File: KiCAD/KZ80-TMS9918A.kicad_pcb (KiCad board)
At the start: 2 copper layers, 100 x 75 mm, 43 parts, among them J1 Conn_Coaxial, J2 SBC8080 BUS, J3 EXT_JP, J4 AD_JP, J5 AD_JP, Q1 2SC1815, U1 74HCT04, U2 74HC139, U3 74HC32, U4 TMS9918A, U5 74HCT04, U6 74HCT574, U7 74HCT574, U8 HM62256, U9 74HCT574, Y1 10.738635MHZ

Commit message: 64k DRAM版 ガーバー出力
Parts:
- removed C15: 470u, Capacitor_THT:CP_Radial_D8.0mm_P3.50mm
- removed the C3 at (139.0, 97.5)
- removed the C4 at (113.5, 94.5)
- removed the C5 at (141.0, 67.5)
- removed the JP1 at (162.0, 105.5)
- removed the U3 at (188.5, 100.5)
- removed U9: 74HCT574, Package_DIP:DIP-20_W7.62mm_Socket
- added C1: 10u, Capacitor_THT:CP_Radial_D5.0mm_P2.50mm, F.Cu at (104.8, 93.5)
- added C14: 0.1u, Capacitor_THT:C_Disc_D3.0mm_W1.6mm_P2.50mm, F.Cu at (197.5, 103.6)
- added C2: 0.1u, Capacitor_THT:C_Disc_D3.0mm_W1.6mm_P2.50mm, F.Cu at (119.0, 66.9)
- added JP2: A7_JP, Connector_PinHeader_2.54mm:PinHeader_1x03_P2.54mm_Vertical, F.Cu at (178.3, 76.9)
- added U4: 74HCT04, Package_DIP:DIP-14_W7.62mm_Socket, F.Cu at (121.8, 86.6)
- C12: value 0.1u -> 10u; footprint Capacitor_THT:C_Disc_D3.0mm_W1.6mm_P2.50mm -> Capacitor_THT:CP_Radial_D5.0mm_P2.50mm
- C13: value 10u -> 0.1u; footprint Capacitor_THT:CP_Radial_D5.0mm_P2.50mm -> Capacitor_THT:C_Disc_D3.0mm_W1.6mm_P2.50mm
- C7: value 0.1u -> 470u; footprint Capacitor_THT:C_Disc_D3.0mm_W1.6mm_P2.50mm -> Capacitor_THT:CP_Radial_D5.0mm_P2.50mm
- L1: value L_Core_Ferrite -> L_Ferrite_Small; footprint Inductor_THT:L_Axial_L5.3mm_D2.2mm_P10.16mm_Horizontal_Vishay_IM-1 -> Resistor_THT:R_Axial_DIN0207_L6.3mm_D2.5mm_P10.16mm_Horizontal
- U1: value 74HCT04 -> 74HCT32
- U2: value 74HC139 -> 74HCT04; footprint Package_DIP:DIP-16_W7.62mm_Socket -> Package_DIP:DIP-14_W7.62mm_Socket
- U5: value 74HCT04 -> 74HCT139; footprint Package_DIP:DIP-14_W7.62mm_Socket -> Package_DIP:DIP-16_W7.62mm_Socket
- U6: value 74HCT574 -> 74HCT244
- U7: value 74HCT574 -> 4464-64k-4bit-DRAM; footprint Package_DIP:DIP-20_W7.62mm_Socket -> Package_DIP:DIP-18_W7.62mm_Socket
- U8: value HM62256 -> 4464-64k-4bit-DRAM; footprint Package_DIP:DIP-28_W15.24mm -> Package_DIP:DIP-18_W7.62mm_Socket
- moved C13 95.3 mm to (197.3, 114.8)
- moved C12 87.9 mm to (116.0, 62.2), turned to 90 degrees
- moved C9 67.6 mm to (119.0, 78.5), turned to -90 degrees
- moved U1 66.8 mm to (121.8, 75.0), turned to 90 degrees
- moved C7 62.8 mm to (103.3, 80.0), turned to 0 degrees
- moved C10 56.9 mm to (140.4, 66.9), turned to -90 degrees
- moved U7 52.6 mm to (174.2, 114.6), turned to 90 degrees
- moved U3 51.8 mm to (120.8, 115.6), turned to 90 degrees
- moved C8 51.3 mm to (138.8, 97.3)
- moved J1 50.2 mm to (110.5, 70.4), turned to 90 degrees
- moved R1 42.8 mm to (115.7, 87.9)
- moved R2 42.3 mm to (112.4, 77.8)
- moved J4 40.3 mm to (165.3, 70.8), turned to 90 degrees
- moved U8 39.6 mm to (174.4, 103.4), turned to 90 degrees
- moved R4 36.4 mm to (111.2, 111.3), turned to 90 degrees
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- renumbered C1 to C3, C14 to C4, C2 to C5, J3 to J2, J2 to J3, JP2 to JP1, R4 to R1, R5 to R2, R1 to R3, R2 to R4, R3 to R5, U4 to U3
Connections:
- C7 pad 1: VCC -> Net-(Q1-E)
- C7 pad 2: GND -> Net-(J1-In)
- J1 pad 1: Net-(C15-Pad2) -> Net-(J1-In)
- J3 pad 17: /~IOR -> /~{IOR}
- J3 pad 18: Net-(J2-Pad18) -> unconnected-(J3-Pin_18-Pad18)
- J3 pad 19: /~IOW -> /~{IOW}
- J3 pad 20: Net-(J2-Pad20) -> unconnected-(J3-Pin_20-Pad20)
- J3 pad 22: Net-(J2-Pad22) -> unconnected-(J3-Pin_22-Pad22)
- J3 pad 24: Net-(J2-Pad24) -> unconnected-(J3-Pin_24-Pad24)
- J3 pad 26: Net-(J2-Pad26) -> unconnected-(J3-Pin_26-Pad26)
- J3 pad 27: Net-(J2-Pad27) -> unconnected-(J3-Pin_27-Pad27)
- J3 pad 33: Net-(J2-Pad33) -> unconnected-(J3-Pin_33-Pad33)
- J3 pad 34: Net-(J2-Pad34) -> unconnected-(J3-Pin_34-Pad34)
- J3 pad 35: Net-(J2-Pad35) -> unconnected-(J3-Pin_35-Pad35)
- J3 pad 36: Net-(J2-Pad36) -> unconnected-(J3-Pin_36-Pad36)
- J3 pad 37: Net-(J2-Pad37) -> unconnected-(J3-Pin_37-Pad37)
- J3 pad 38: Net-(J2-Pad38) -> unconnected-(J3-Pin_38-Pad38)
- J3 pad 39: Net-(J2-Pad39) -> unconnected-(J3-Pin_39-Pad39)
- J3 pad 40: Net-(J2-Pad40) -> unconnected-(J3-Pin_40-Pad40)
- J3 pad 5: Net-(J2-Pad5) -> unconnected-(J3-Pin_5-Pad5)
- J3 pad 6: Net-(J2-Pad6) -> unconnected-(J3-Pin_6-Pad6)
- J3 pad 7: Net-(J2-Pad7) -> unconnected-(J3-Pin_7-Pad7)
- J4 pad 1: Net-(J4-Pad1) -> Net-(J4-Pin_1)
- J4 pad 2: Net-(J4-Pad2) -> Net-(J4-Pin_2)
- J4 pad 3: Net-(J4-Pad3) -> Net-(J4-Pin_3)
- J4 pad 4: Net-(J4-Pad2) -> Net-(J4-Pin_2)
- J4 pad 5: Net-(J4-Pad5) -> Net-(J4-Pin_5)
- J4 pad 6: Net-(J4-Pad2) -> Net-(J4-Pin_2)
- J4 pad 7: Net-(J4-Pad7) -> Net-(J4-Pin_7)
- J4 pad 8: Net-(J4-Pad2) -> Net-(J4-Pin_2)
- J5 pad 1: Net-(J5-Pad1) -> Net-(J5-Pin_1)
- J5 pad 2: Net-(J5-Pad2) -> Net-(J5-Pin_2)
- J5 pad 3: Net-(J5-Pad3) -> Net-(J5-Pin_3)
- J5 pad 4: Net-(J5-Pad2) -> Net-(J5-Pin_2)
- J5 pad 5: Net-(J5-Pad5) -> Net-(J5-Pin_5)
- J5 pad 6: Net-(J5-Pad2) -> Net-(J5-Pin_2)
- J5 pad 7: Net-(J5-Pad7) -> Net-(J5-Pin_7)
- J5 pad 8: Net-(J5-Pad2) -> Net-(J5-Pin_2)
- JP1 pad 2: Net-(JP2-Pad2) -> Net-(JP1-C)
- Q1 pad 1: Net-(C15-Pad1) -> Net-(Q1-E)
- R1 pad 2: Net-(C15-Pad2) -> Net-(J1-In)
- R2 pad 1: Net-(C15-Pad2) -> Net-(J1-In)
- R3 pad 1: Net-(C15-Pad1) -> Net-(Q1-E)
- U1 pad 1: /R~W -> Net-(J4-Pin_2)
- U1 pad 10: /COL -> GND
- U1 pad 11: Net-(U1-Pad11) -> unconnected-(U1-Pad11)
- U1 pad 12: Net-(JP2-Pad2) -> GND
- U1 pad 13: /~INT -> GND
- U1 pad 2: /~R~W -> /~{IOR}
- U1 pad 3: /~RAS -> /~{CSR}
- U1 pad 4: /ROW -> Net-(J4-Pin_2)
- U1 pad 5: /~CAS -> /~{IOW}
- U1 pad 6: Net-(U1-Pad6) -> /~{CSW}
- U1 pad 8: Net-(U1-Pad11) -> unconnected-(U1-Pad8)
- U1 pad 9: Net-(U1-Pad6) -> GND
- U2 pad 1: Net-(JP1-Pad2) -> /R~{W}
- U2 pad 10: Net-(J4-Pad5) -> Net-(U2-Pad10)
- U2 pad 11: Net-(J4-Pad3) -> Net-(U2-Pad11)
- U2 pad 12: Net-(J4-Pad1) -> /W
- U2 pad 13: /A4 -> Net-(U2-Pad10)
- U2 pad 14: /A3 -> VCC
- U2 pad 2: /A5 -> /G
- U2 pad 3: /A6 -> /G
- U2 pad 4: Net-(J5-Pad1) -> /OE
- U2 pad 5: Net-(J5-Pad3) -> /OE
- U2 pad 6: Net-(J5-Pad5) -> Net-(U2-Pad6)
- U2 pad 7: Net-(J5-Pad7) -> GND
- U2 pad 8: GND -> Net-(U2-Pad11)
- U2 pad 9: Net-(J4-Pad7) -> Net-(U2-Pad6)
- U3 pad 1: /~RAS -> /~{RAS}
- U3 pad 11: /R~W -> /R~{W}
- U3 pad 14: /~CSW -> /~{CSW}
- U3 pad 15: /~CSR -> /~{CSR}
- U3 pad 16: /~INT -> /~{INT}
- U3 pad 2: /~CAS -> /~{CAS}
- U3 pad 34: /~RES -> /~{RES}
- U5 pad 1: /A7 -> Net-(JP2-C)
- U5 pad 10: Net-(U5-Pad10) -> Net-(J4-Pin_5)
- U5 pad 11: GND -> Net-(J4-Pin_3)
- U5 pad 12: Net-(U5-Pad12) -> Net-(J4-Pin_1)
- U5 pad 13: GND -> /A4
- U5 pad 14: VCC -> /A3
- U5 pad 2: Net-(JP1-Pad3) -> /A5
- U5 pad 3: /RES -> /A6
- U5 pad 4: /~RES -> Net-(J5-Pin_1)
- U5 pad 5: GND -> Net-(J5-Pin_3)
- U5 pad 6: Net-(U5-Pad6) -> Net-(J5-Pin_5)
- U5 pad 7: GND -> Net-(J5-Pin_7)
- U5 pad 8: Net-(U5-Pad8) -> GND
- U5 pad 9: GND -> Net-(J4-Pin_7)
- U6 pad 1: /R~W -> /OE
- U6 pad 11: /~R~W -> /AD4
- U6 pad 12: /VD7 -> /VD3
- U6 pad 13: /VD6 -> /AD5
- U6 pad 14: /VD5 -> /VD2
- U6 pad 15: /VD4 -> /AD6
- U6 pad 16: /VD3 -> /VD1
- U6 pad 17: /VD2 -> /AD7
- U6 pad 18: /VD1 -> /VD0
- U6 pad 19: /VD0 -> /OE
- U6 pad 3: /AD1 -> /VD7
- U6 pad 4: /AD2 -> /AD1
- U6 pad 5: /AD3 -> /VD6
- U6 pad 6: /AD4 -> /AD2
- U6 pad 7: /AD5 -> /VD5
- U6 pad 8: /AD6 -> /AD3
- U6 pad 9: /AD7 -> /VD4
- U7 pad 1: GND -> /G
- U7 pad 11: /ROW -> /AD4
- U7 pad 12: /VA6 -> /AD5
- U7 pad 13: /VA5 -> /AD6
- U7 pad 14: /VA4 -> /AD7
- U7 pad 15: /VA3 -> /VD2
- U7 pad 16: /VA2 -> /~{CAS}
- U7 pad 17: /VA1 -> /VD3
- U7 pad 18: /VA0 -> GND
- U7 pad 2: /AD0 -> /VD0
- U7 pad 3: /AD1 -> /VD1
- U7 pad 4: /AD2 -> /W
- U7 pad 5: /AD3 -> /~{RAS}
- U7 pad 6: /AD4 -> /AD1
- U7 pad 7: /AD5 -> /AD2
- U7 pad 8: /AD6 -> /AD3
- U7 pad 9: /AD7 -> VCC
- U8 pad 1: /VA13 -> /G
- U8 pad 10: /VA0 -> GND
- U8 pad 11: /VD0 -> /AD4
- U8 pad 12: /VD1 -> /AD5
- U8 pad 13: /VD2 -> /AD6
- U8 pad 14: GND -> /AD7
- U8 pad 15: /VD3 -> /VD6
- U8 pad 16: /VD4 -> /~{CAS}
- U8 pad 17: /VD5 -> /VD7
- U8 pad 18: /VD6 -> GND
- U8 pad 2: /VA12 -> /VD4
- U8 pad 3: /VA7 -> /VD5
- U8 pad 4: /VA6 -> /W
- U8 pad 5: /VA5 -> /~{RAS}
- U8 pad 6: /VA4 -> /AD1
- U8 pad 7: /VA3 -> /AD2
- U8 pad 8: /VA2 -> /AD3
- U8 pad 9: /VA1 -> VCC
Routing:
- net /~CAS: track 140.1 -> 0.00 mm
- net /~INT: track 123.4 -> 0.00 mm
- net /R~W: track 123.3 -> 0.00 mm, vias 1 -> 0
- net /~RAS: track 109.3 -> 0.00 mm
- net /~CSR: track 105.4 -> 0.00 mm
- net /~IOR: track 105.3 -> 0.00 mm
- net /~CSW: track 103.2 -> 0.00 mm
- net /~IOW: track 99.3 -> 0.00 mm
- net /A4: track 107.1 -> 13.8 mm
- net /~{RAS}: track 0.00 -> 78.3 mm, vias 0 -> 1
- net /W: track 0.00 -> 74.7 mm, vias 0 -> 2
- net /~{CAS}: track 0.00 -> 73.3 mm
- net Net-(JP1-C): track 0.00 -> 66.8 mm
- net /~R~W: track 66.4 -> 0.00 mm
- net /~{CSR}: track 0.00 -> 62.7 mm
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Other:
- net class BOLD removed
- net class Default removed
- board text added: "10uF"
- board text added: "2SC1815"
- board text added: "4464 (DRAM)"
- board text added: "470uF"
- board text added: "74HCT244"
- board text added: "J2"
- board text added: "KUNI-NET 2024"
- board text added: "KZ80-TMS9918A (64k DRAM)"
- board text removed: "74HCT574"
- board text removed: "J3"
- board text removed: "KZ80-TMS9918A REV1"
- board text removed: "SRAM(32k)"

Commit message: シルク印刷間違い修正(64bit、16kbit両方) REV1.1ガーバー出力
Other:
- board text added: "KZ80-TMS9918A (64k DRAM) REV1.1"
- board text removed: "KZ80-TMS9918A (64k DRAM)"
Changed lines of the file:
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@@
     (effects (font (size 1 1) (thickness 0.15)))
   )
-  (gr_text "KZ80-TMS9918A (64k DRAM) " (at 167.056 120.174) (layer "F.SilkS")
-    (effects (font (size 1.5 1.5) (thickness 0.3)))
+  (gr_text "KZ80-TMS9918A (64k DRAM) REV1.1" (at 165.6 120.5) (layer "F.SilkS")
+    (effects (font (size 1.5 1.5) (thickness 0.25) bold))
   )
   (gr_text "74HC139" (at 152.07 71.152) (layer "F.SilkS")
@@
     (effects (font (size 1 1) (thickness 0.15)))
   )
-  (gr_text "80" (at 183.338 80.186) (layer "F.SilkS")
+  (gr_text "80" (at 178.4 79.7) (layer "F.SilkS")
     (effects (font (size 1 1) (thickness 0.15)))
   )
@@
     (effects (font (size 1 1) (thickness 0.15)) (justify left bottom))
   )
-  (gr_text "00" (at 178.088 80.186) (layer "F.SilkS")
+  (gr_text "00" (at 183 79.7) (layer "F.SilkS")
     (effects (font (size 1 1) (thickness 0.15)))
   )

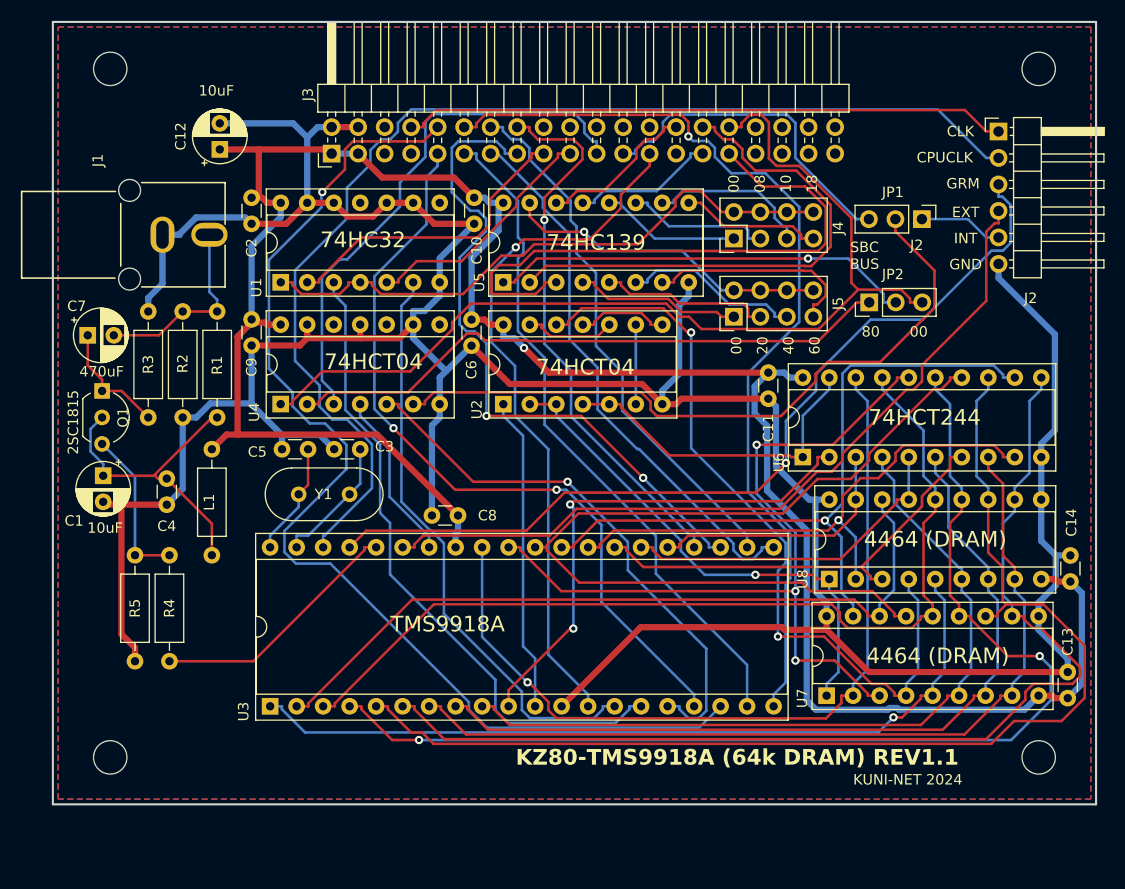
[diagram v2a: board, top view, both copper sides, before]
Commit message: 64k版 部品配置調整、16k版 4164 DRAM対応版 ガーバーデータ出力
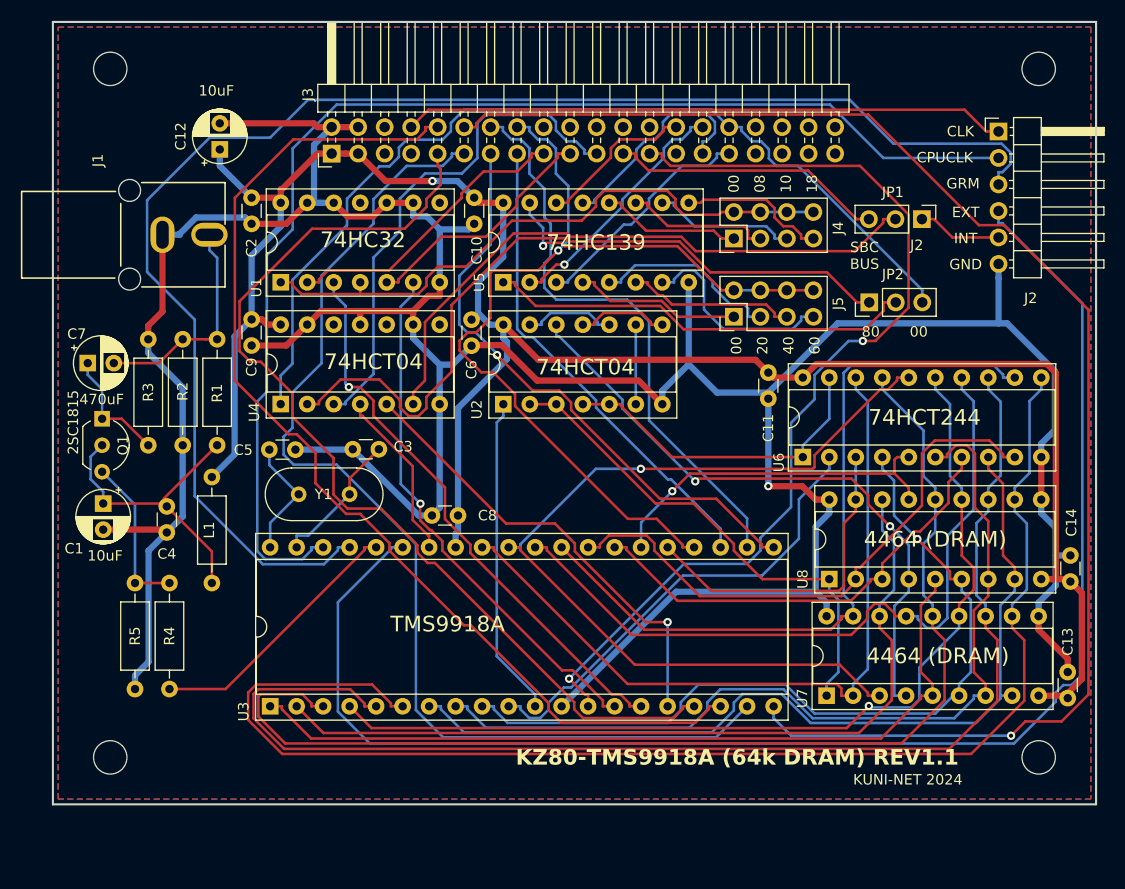
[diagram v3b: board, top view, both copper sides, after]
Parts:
- moved C5 3.71 mm to (120.8, 91.0), turned to 0 degrees
- moved C1 2.66 mm to (104.8, 96.2)
- moved C7 2.66 mm to (103.3, 82.7)
- moved L1 2.66 mm to (115.2, 93.6)
- moved Q1 2.66 mm to (104.7, 88.0)
- moved R1 2.66 mm to (115.7, 90.6)
- moved R2 2.66 mm to (112.4, 80.4)
- moved R3 2.66 mm to (109.1, 90.6)
- moved R5 2.66 mm to (107.9, 103.8)
- moved C4 2.66 mm to (110.9, 96.4)
- moved R4 2.66 mm to (111.2, 113.9)
- moved C3 1.79 mm to (131.2, 91.0)
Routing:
- net /EXTVDP: track 76.5 -> 142.8 mm
- net /GROMCLK: track 85.0 -> 141.3 mm, vias 1 -> 0
- net /D3: track 90.0 -> 138.8 mm
- net /D2: track 65.3 -> 104.9 mm
- net /A6: track 56.9 -> 22.5 mm
- net /A0: track 66.8 -> 94.0 mm, vias 1 -> 2
- net /AD4: track 103.7 -> 130.2 mm
- net /A5: track 50.3 -> 24.1 mm, vias 0 -> 1
- net /AD7: track 90.4 -> 111.8 mm
- net /D0: track 74.4 -> 95.2 mm, vias 2 -> 0
- net /D6: track 65.1 -> 46.4 mm, vias 2 -> 0
- net /AD6: track 109.2 -> 91.3 mm, vias 2 -> 1
- net VCC: track 216.6 -> 199.1 mm
- net /VD2: track 85.8 -> 71.1 mm
- net /W: track 74.7 -> 60.6 mm
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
